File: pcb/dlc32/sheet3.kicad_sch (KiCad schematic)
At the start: 3 parts, among them J17 X endstop, J18 X1, J19 X2

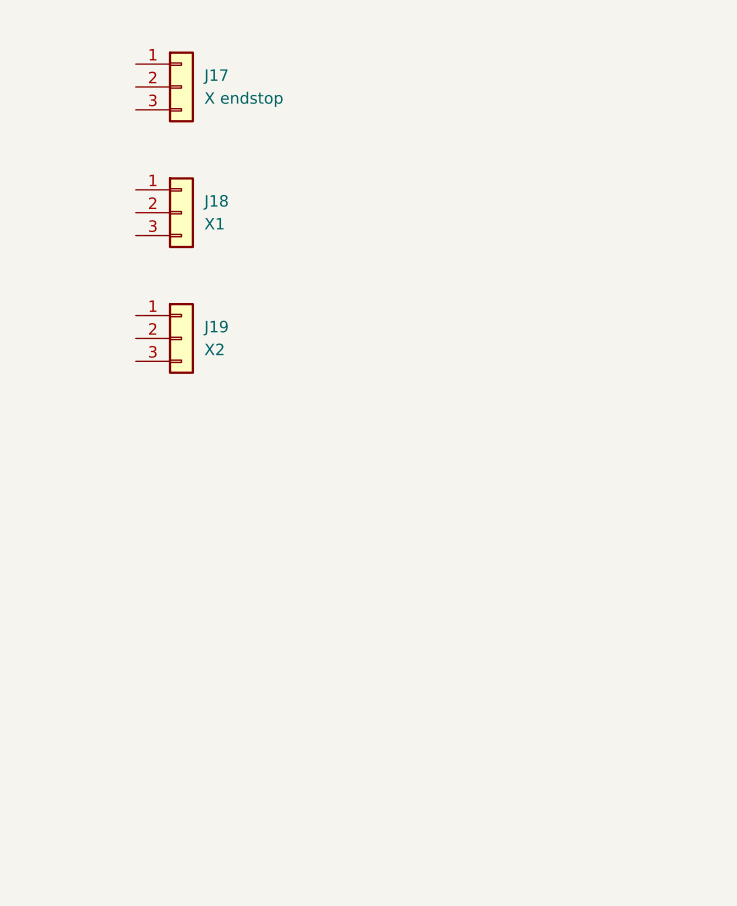
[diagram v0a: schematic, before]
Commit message: Add support for dual endstops.
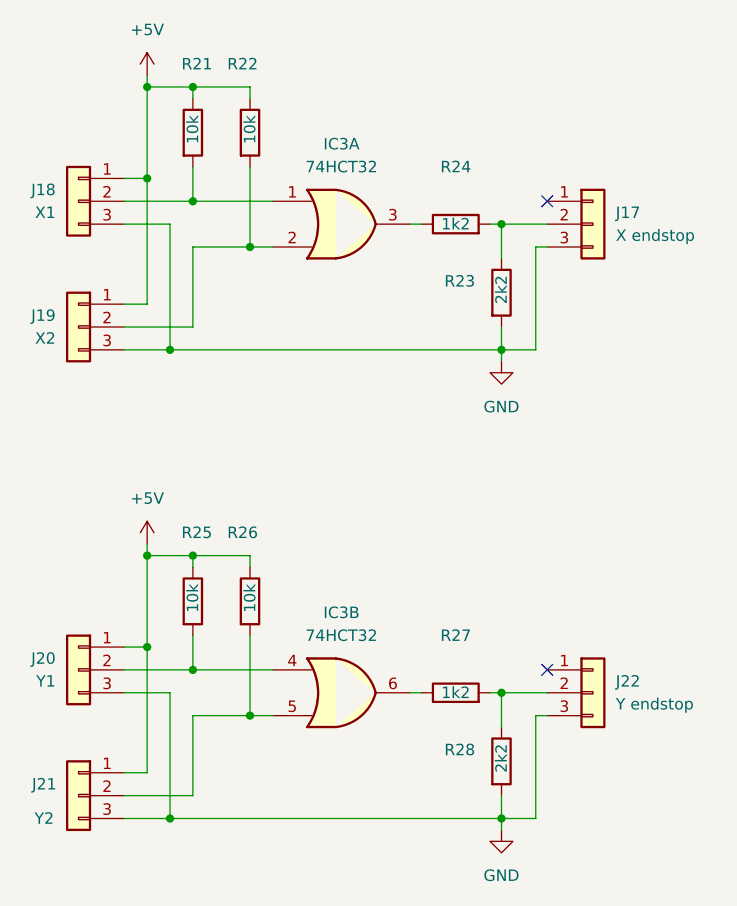
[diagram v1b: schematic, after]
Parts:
- added IC3: 74HCT32, PCM_Package_SO_AKL:SOIC-14_3.9x8.7mm_P1.27mm, symbol 74xx:74LS32
- added J20: Y1, Connector_JST:JST_XH_B3B-XH-A_1x03_P2.50mm_Vertical, symbol Connector_Generic:Conn_01x03
- added J21: Y2, Connector_JST:JST_XH_B3B-XH-A_1x03_P2.50mm_Vertical, symbol Connector_Generic:Conn_01x03
- added J22: Y endstop, Connector_JST:JST_XH_B3B-XH-A_1x03_P2.50mm_Vertical, symbol Connector_Generic:Conn_01x03
- added R21, R22, R25, R26: 10k, PCM_Resistor_SMD_AKL:R_0603_1608Metric, symbol Device:R
- added R23, R28: 2k2, PCM_Resistor_SMD_AKL:R_0603_1608Metric, symbol Device:R
- added R24, R27: 1k2, PCM_Resistor_SMD_AKL:R_0603_1608Metric, symbol Device:R
- J17, J18, J19: footprint (none) -> Connector_JST:JST_XH_B3B-XH-A_1x03_P2.50mm_Vertical
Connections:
- net at J17.2 (Pin_2): now also R23.1, R24.2
- net GND: now reaches J17.3 (Pin_3)
- net GND: now also J18.3 (Pin_3), J19.3 (Pin_3), J20.3 (Pin_3), J21.3 (Pin_3), J22.3 (Pin_3), R23.2, R28.2
- net +5V: now reaches J18.1 (Pin_1)
- net +5V: now also J19.1 (Pin_1), J20.1 (Pin_1), J21.1 (Pin_1), R21.1, R22.1, R25.1, R26.1
- net at J18.2 (Pin_2): now also IC3.1, R21.2
- net at J19.2 (Pin_2): now also IC3.2, R22.2
- new net: IC3.6, R27.1
- new net: J22.2 (Pin_2), R27.2, R28.1
- new net: IC3.4, J20.2 (Pin_2), R25.2
- new net: IC3.3, R24.1
- new net: IC3.5, J21.2 (Pin_2), R26.2
- no-connect marks 0 -> 2
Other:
- moved on the sheet: J17, J18, J19
